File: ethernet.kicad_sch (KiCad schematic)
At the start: 4 parts, among them J3 PinHeader_2x5_P1.27mm_SMD, U1 MPFS250T-FCVG484, U2 SDINBDG4-8G, U4 MT25QL01GBBB8E_SOP2-16

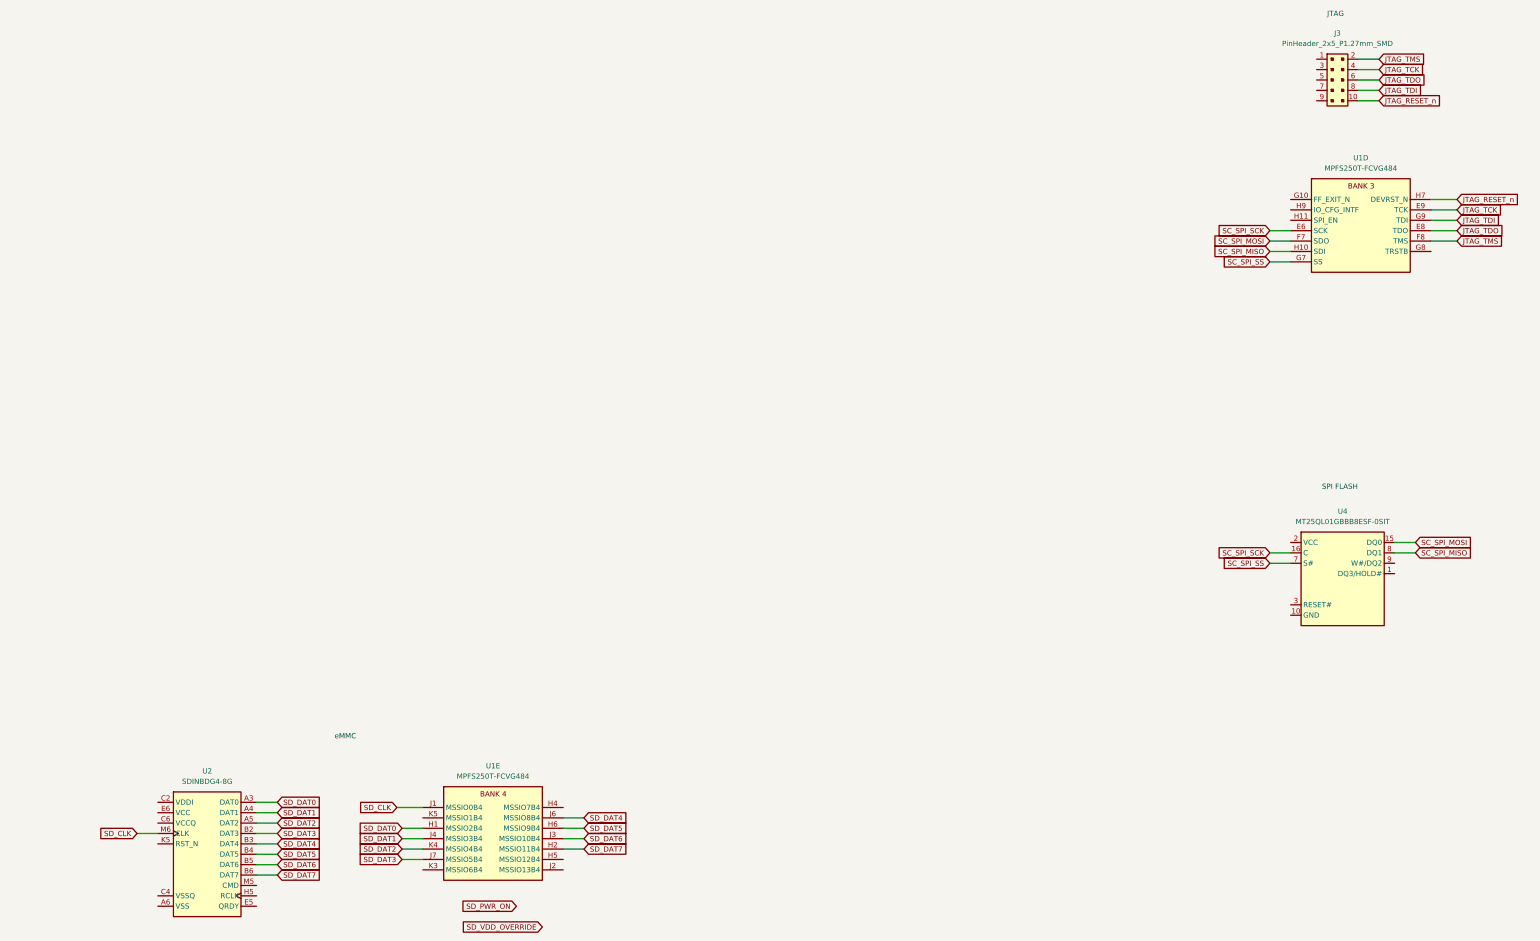
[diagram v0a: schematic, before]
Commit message: [#53847] Add PCLK to Crosslink data transmission
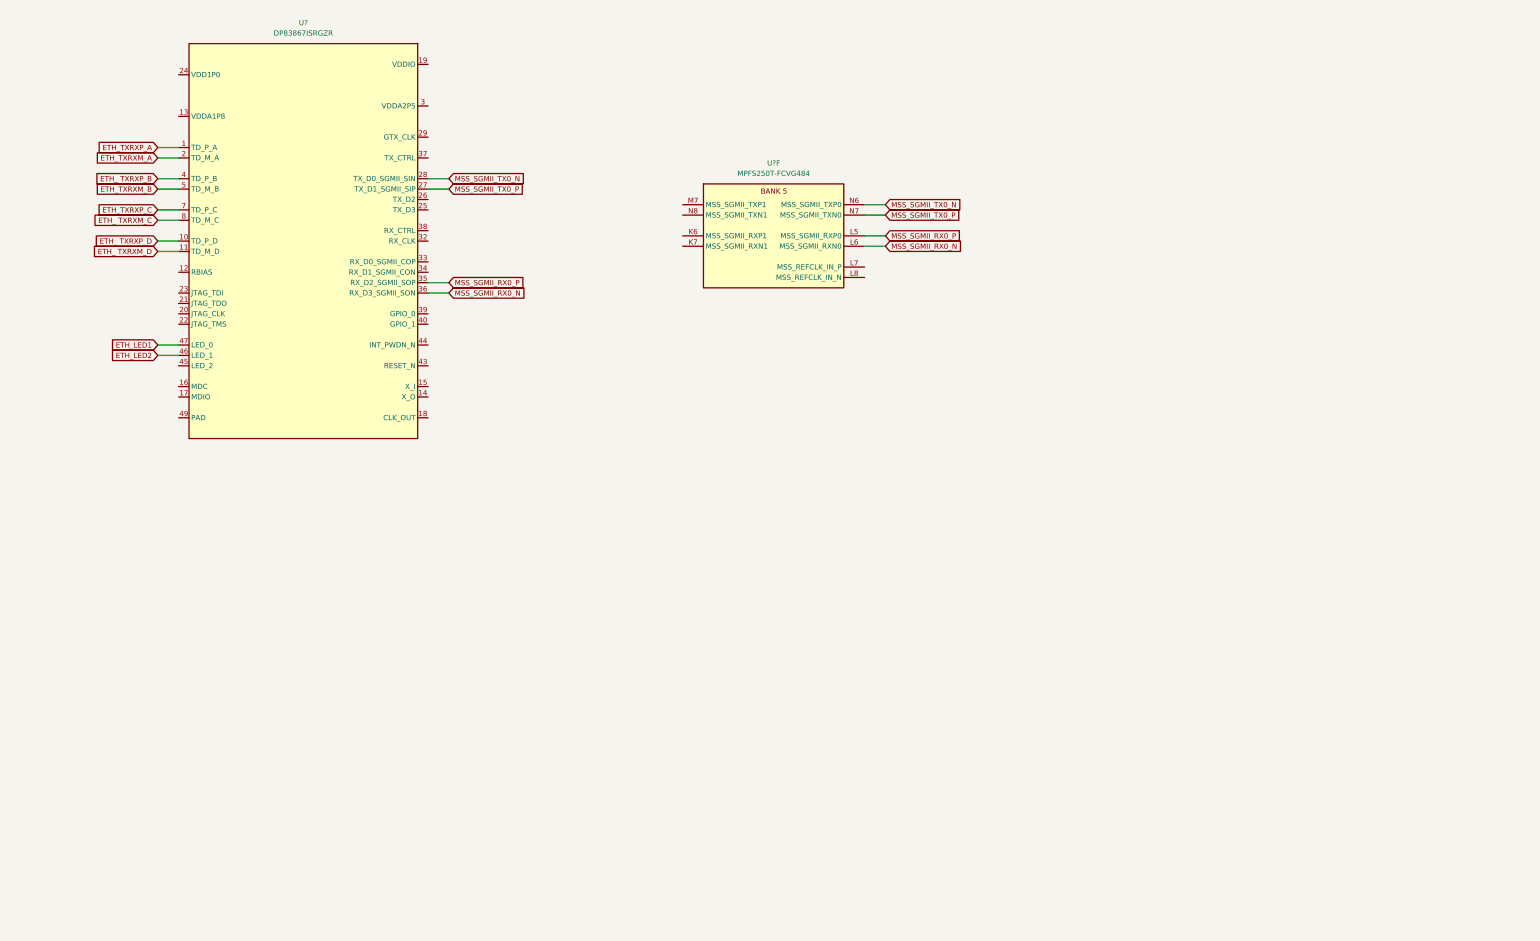
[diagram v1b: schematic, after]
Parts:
- removed J3: PinHeader_2x5_P1.27mm_SMD, antmicro-footprints:PinHeader_2x5_P1.27mm_SMD, symbol antmicroGenericPinHeaders:PinHeader_2x5_P1.27mm_SMD
- removed U1: MPFS250T-FCVG484, antmicro-footprints:BGA-484_19x19mm_Layout22x22_P0.8mm_FCVG484, symbol antmicroMicrocontrollers:MPFS250T-FCVG484
- removed U2: SDINBDG4-8G, antmicro-footprints:BGA-196-153_11.5x13mm_Layout14x14_P0.5x0.5mm, symbol antmicroMemory:SDINBDG4-8G
- removed U4: MT25QL01GBBB8E_SOP2-16, antmicro-footprints:SOP2-16_7.5x10.3mm, symbol antmicroMemory:MT25QL01GBBB8E_SOP2-16
- added U?: DP83867ISRGZR, antmicro-footprints:VQFN-48_7x7mm_P0.5mm_EP4.1x4.1mm, symbol antmicroInterfaceControllers:DP83867ISRGZR
- added U?: MPFS250T-FCVG484, antmicro-footprints:BGA-484_19x19mm_Layout22x22_P0.8mm_FCVG484, symbol antmicroMicrocontrollers:MPFS250T-FCVG484
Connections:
- new net: U?.13 (VDDA1P8), U?.48 (VDDA1P8)
- new net: U?.19 (VDDIO), U?.30 (VDDIO), U?.41 (VDDIO)
- new net: U?.24 (VDD1P0), U?.31 (VDD1P0), U?.42 (VDD1P0), U?.6 (VDD1P0)
- new net: U?.3 (VDDA2P5), U?.9 (VDDA2P5)
- new net ETH_ TXRXM_C: U?.8 (TD_M_C)
- new net ETH_ TXRXM_D: U?.11 (TD_M_D)
- new net ETH_ TXRXP_B: U?.4 (TD_P_B)
- new net ETH_ TXRXP_D: U?.10 (TD_P_D)
- new net ETH_LED1: U?.47 (LED_0)
- new net ETH_LED2: U?.46 (LED_1)
- new net ETH_TXRXM_A: U?.2 (TD_M_A)
- new net ETH_TXRXM_B: U?.5 (TD_M_B)
- new net ETH_TXRXP_A: U?.1 (TD_P_A)
- new net ETH_TXRXP_C: U?.7 (TD_P_C)
- new net MSS_SGMII_RX0_N: U?.36 (RX_D3_SGMII_SON), U?.L6 (MSS_SGMII_RXN0)
- new net MSS_SGMII_RX0_P: U?.35 (RX_D2_SGMII_SOP), U?.L5 (MSS_SGMII_RXP0)
- new net MSS_SGMII_TX0_N: U?.28 (TX_D0_SGMII_SIN), U?.N6 (MSS_SGMII_TXP0)
- new net MSS_SGMII_TX0_P: U?.27 (TX_D1_SGMII_SIP), U?.N7 (MSS_SGMII_TXN0)
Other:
- note removed: "JTAG"
- note removed: "SPI FLASH"
- note removed: "eMMC"

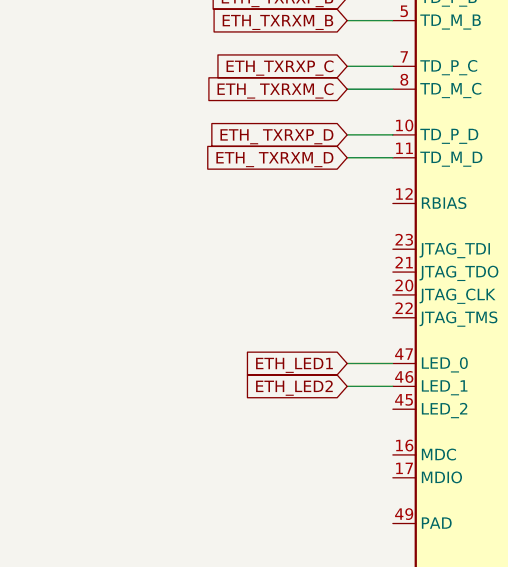
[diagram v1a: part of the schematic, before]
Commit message: [#53979] Add 2-lane CSI transceiver resistor array
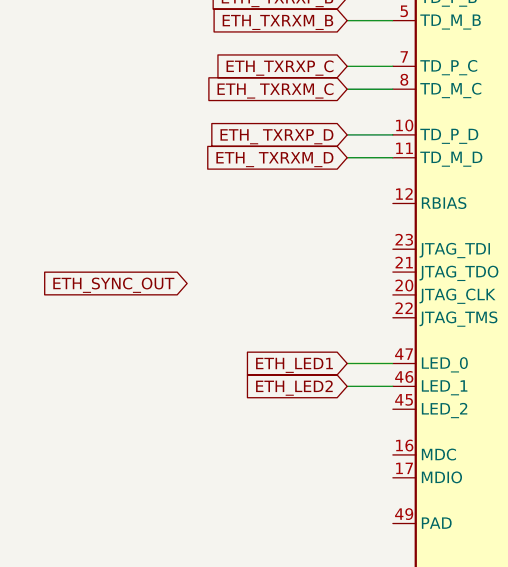
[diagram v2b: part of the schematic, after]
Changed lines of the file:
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@@
     (stroke (width 0) (type default) (color 0 0 0 0))
+  )
+  (global_label "ETH_SYNC_OUT" (shape input) (at 34.29 110.49 180) (fields_autoplaced)
+    (effects (font (size 1.27 1.27)) (justify right))
+    (property "Intersheet References" "${INTERSHEET_REFS}" (id 0) (at 17.9674 110.4106 0)
+      (effects (font (size 1.27 1.27)) (justify right) hide)
+    )
   )
   (global_label "ETH_LED2" (shape input) (at 52.07 121.92 180) (fields_autoplaced)

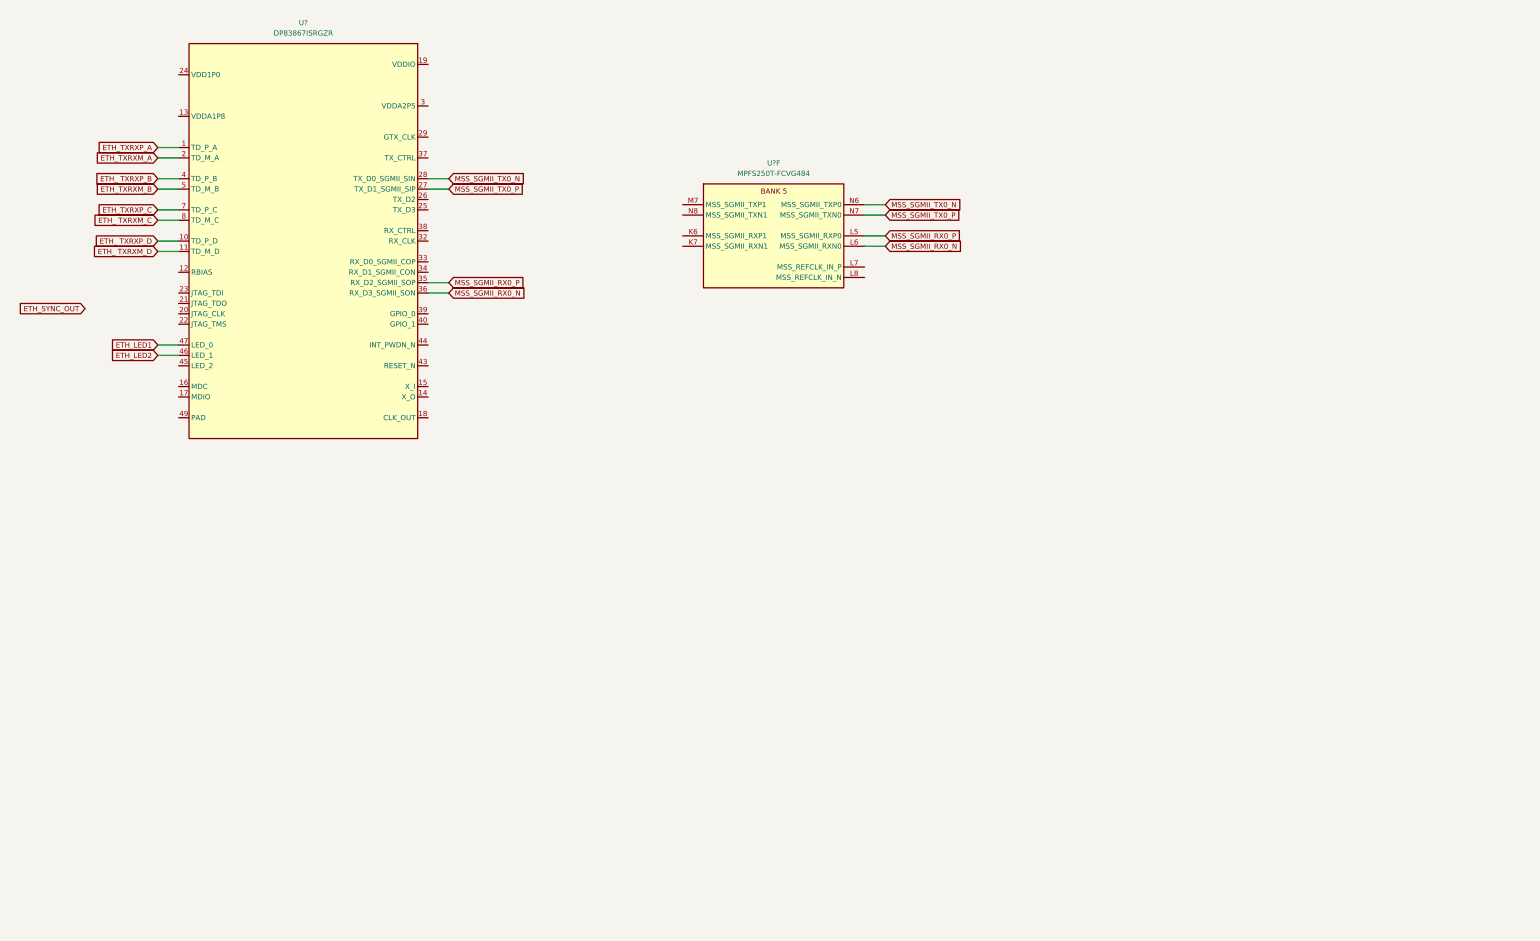
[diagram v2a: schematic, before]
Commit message: [#54084] Sheets cleanup
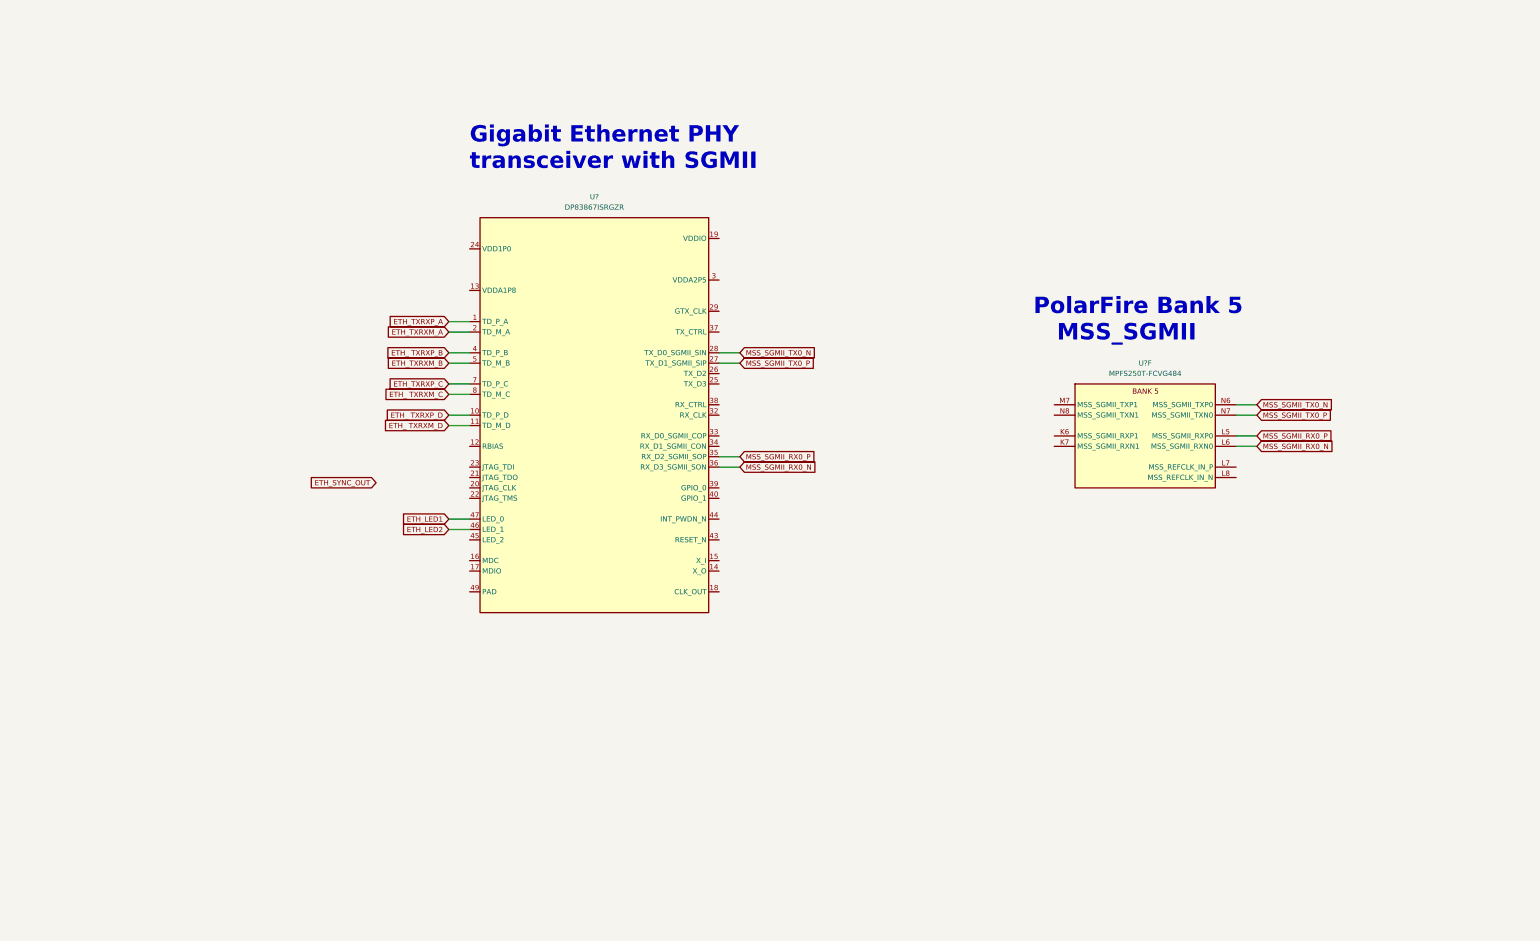
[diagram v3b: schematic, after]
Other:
- note added: "Gigabit Ethernet PHY transceiver with SGMII"
- note added: "PolarFire Bank 5 MSS_SGMII"
- company: (none) -> Antmicro Ltd
- title: (none) -> PolarFire SoM
- moved on the sheet: U?, U?F

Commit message: [#54016] Connect power to Ethernet PHY
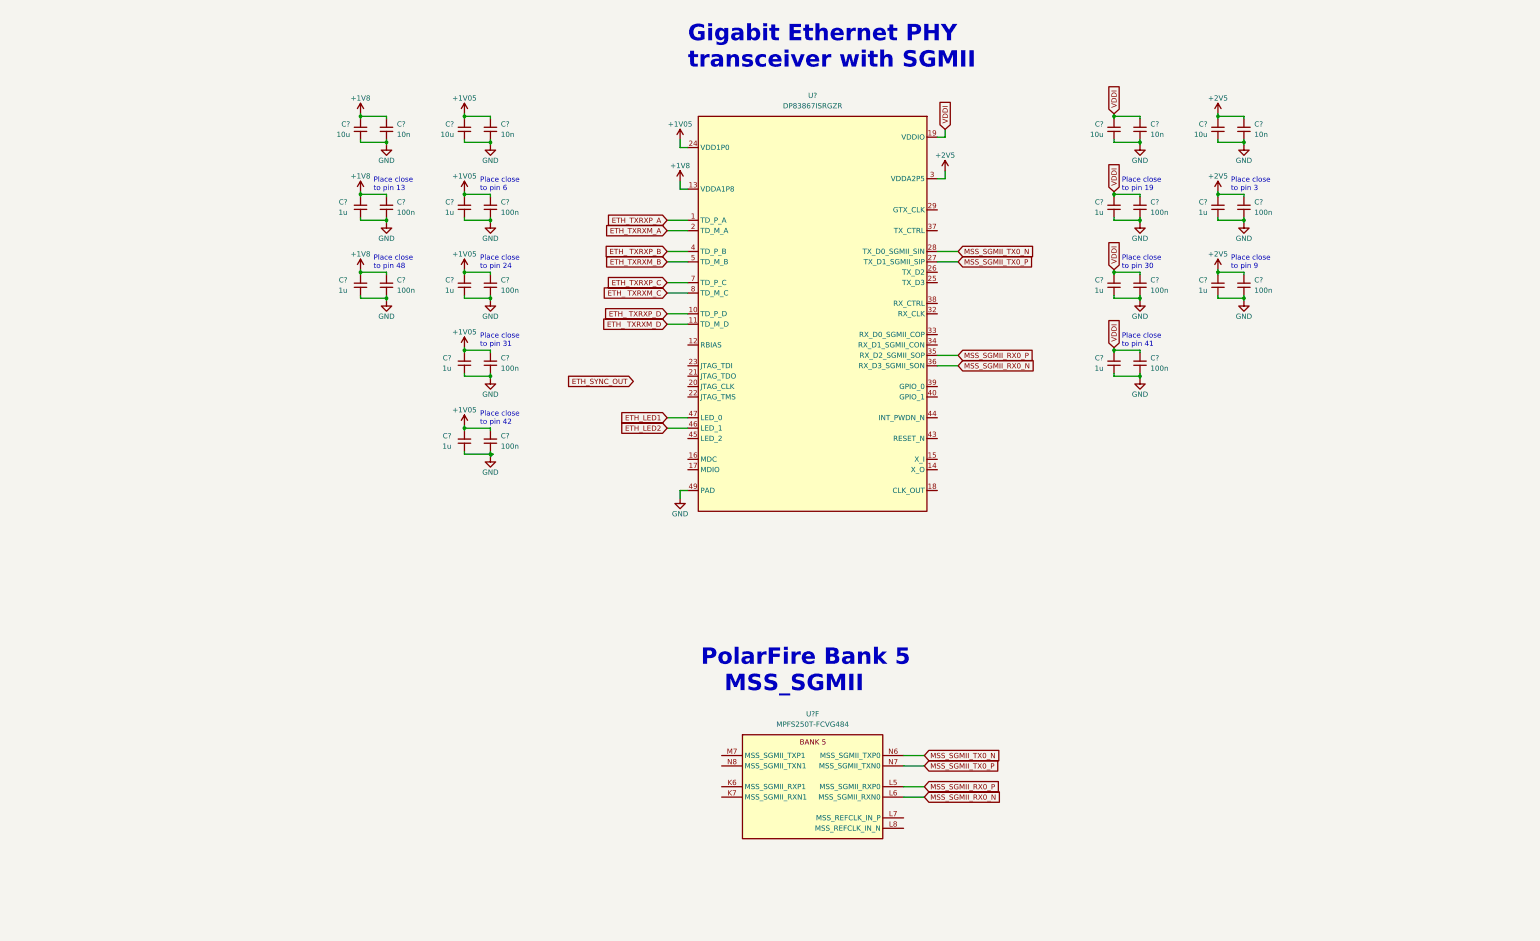
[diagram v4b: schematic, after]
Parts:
- added C? (x11): C_1u_0402, antmicro-footprints:C_0402_1005Metric, symbol antmicroCapacitors0402:C_1u_0402
- added C? (x4): C_10n_0402, antmicro-footprints:C_0402_1005Metric, symbol antmicroCapacitors0402:C_10n_0402
- added C? (x11): C_100n_0402, antmicro-footprints:C_0402_1005Metric, symbol antmicroCapacitors0402:C_100n_0402
- added C? (x4): C_10u_0402, antmicro-footprints:C_0402_1005Metric, symbol antmicroCapacitors0402:C_10u_0402
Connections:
- net +1V8: now reaches U?.13 (VDDA1P8), U?.48 (VDDA1P8)
- net +1V8: now also C?.2, C?.2, C?.2, C?.2, C?.2, C?.2
- net VDDI: now reaches U?.19 (VDDIO), U?.30 (VDDIO), U?.41 (VDDIO)
- net VDDI: now also C?.2, C?.2, C?.2, C?.2, C?.2, C?.2, C?.2, C?.2
- net +1V05: now reaches U?.24 (VDD1P0), U?.31 (VDD1P0), U?.42 (VDD1P0), U?.6 (VDD1P0)
- net +1V05: now also C?.2, C?.2, C?.2, C?.2, C?.2, C?.2, C?.2, C?.2, C?.2, C?.2
- net +2V5: now reaches U?.3 (VDDA2P5), U?.9 (VDDA2P5)
- net +2V5: now also C?.2, C?.2, C?.2, C?.2, C?.2, C?.2
- net GND: now reaches U?.49 (PAD)
- net GND: now also C?.1, C?.1, C?.1, C?.1, C?.1, C?.1, C?.1, C?.1, C?.1, C?.1, C?.1, C?.1, C?.1, C?.1, C?.1, C?.1, C?.1, C?.1, C?.1, C?.1, C?.1, C?.1, C?.1, C?.1, C?.1, C?.1, C?.1, C?.1, C?.1, C?.1
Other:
- note added: "Place close to pin 13"
- note added: "Place close to pin 19"
- note added: "Place close to pin 24"
- note added: "Place close to pin 3"
- note added: "Place close to pin 30"
- note added: "Place close to pin 31"
- note added: "Place close to pin 41"
- note added: "Place close to pin 42"
- note added: "Place close to pin 48"
- note added: "Place close to pin 6"
- note added: "Place close to pin 9"
- moved on the sheet: U?, U?F
